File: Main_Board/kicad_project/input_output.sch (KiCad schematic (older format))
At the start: 70 parts

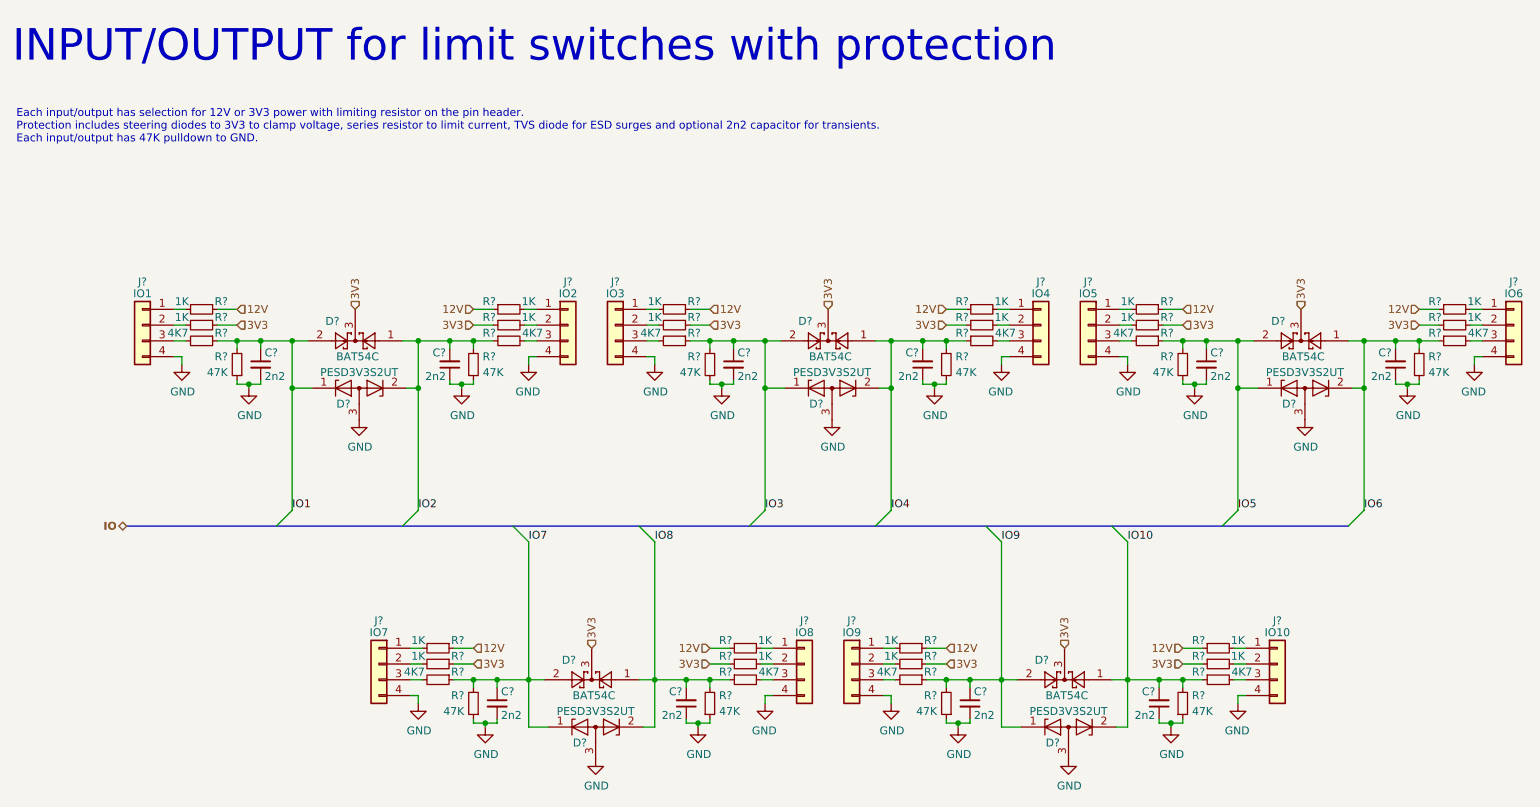
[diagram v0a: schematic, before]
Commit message: Fix I/O protection
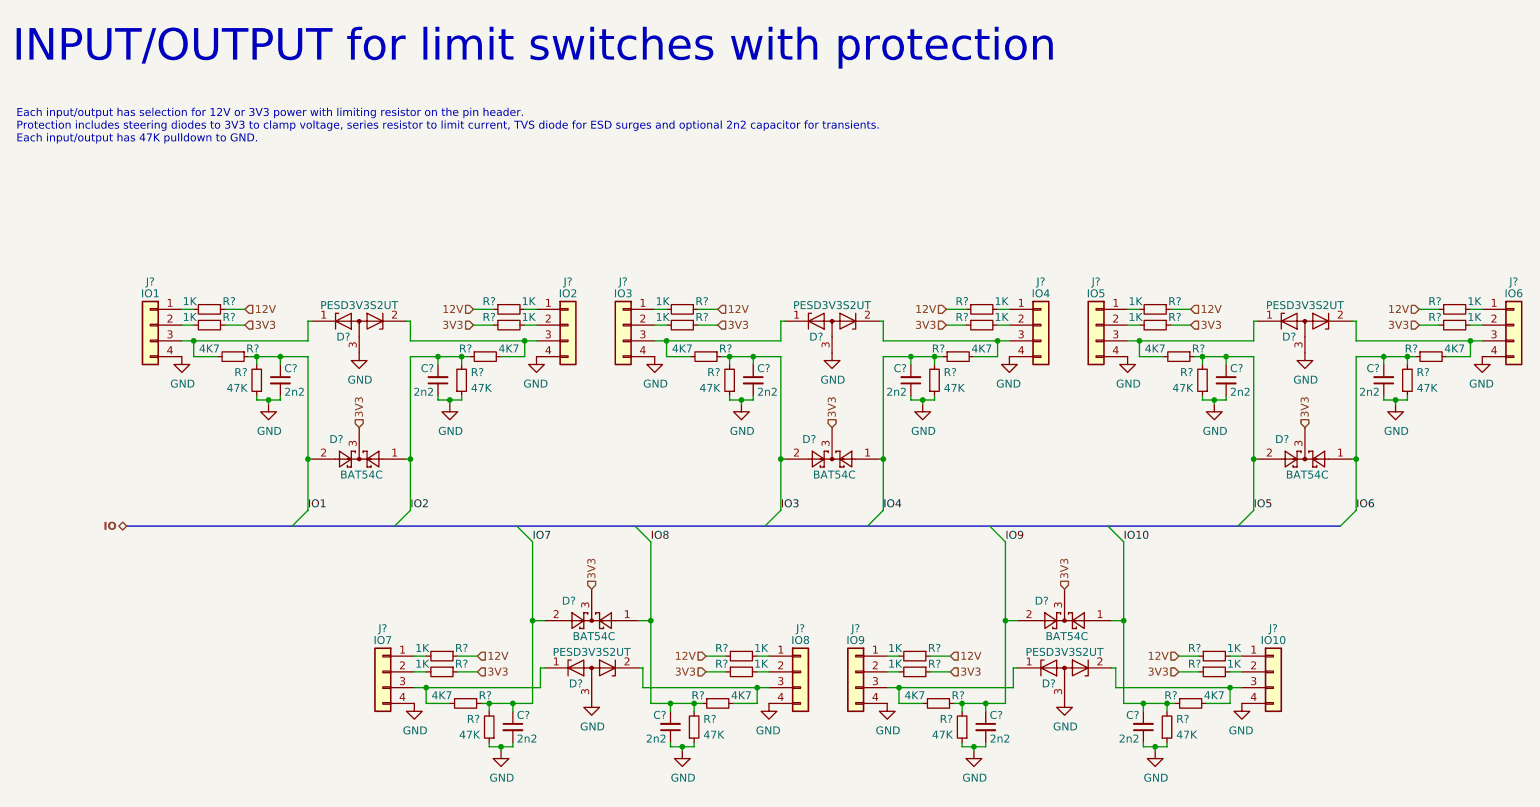
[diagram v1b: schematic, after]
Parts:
- removed C? (x8): 2n2, Capacitor_SMD:C_0603_1608Metric, symbol Device:C_Small
- removed D? (x4): BAT54C, Package_TO_SOT_SMD:SOT-23, symbol Diode:BAT54C
- removed D? (x4): PESD3V3S2UT, Package_TO_SOT_SMD:SOT-23, symbol Device:D_Zener_x2_ACom_KKA
- removed J?: IO3, Connector_PinHeader_2.54mm:PinHeader_1x04_P2.54mm_Vertical, symbol Connector_Generic:Conn_01x04
- removed J?: IO4, Connector_PinHeader_2.54mm:PinHeader_1x04_P2.54mm_Vertical, symbol Connector_Generic:Conn_01x04
- removed J?: IO5, Connector_PinHeader_2.54mm:PinHeader_1x04_P2.54mm_Vertical, symbol Connector_Generic:Conn_01x04
- removed J?: IO6, Connector_PinHeader_2.54mm:PinHeader_1x04_P2.54mm_Vertical, symbol Connector_Generic:Conn_01x04
- removed J?: IO7, Connector_PinHeader_2.54mm:PinHeader_1x04_P2.54mm_Vertical, symbol Connector_Generic:Conn_01x04
- removed J?: IO8, Connector_PinHeader_2.54mm:PinHeader_1x04_P2.54mm_Vertical, symbol Connector_Generic:Conn_01x04
- removed J?: IO9, Connector_PinHeader_2.54mm:PinHeader_1x04_P2.54mm_Vertical, symbol Connector_Generic:Conn_01x04
- removed J?: IO10, Connector_PinHeader_2.54mm:PinHeader_1x04_P2.54mm_Vertical, symbol Connector_Generic:Conn_01x04
- removed R? (x16): 1K, Resistor_SMD:R_0603_1608Metric, symbol Device:R_Small
- removed R? (x8): 4K7, Resistor_SMD:R_0603_1608Metric, symbol Device:R_Small
- removed R? (x8): 47K, Resistor_SMD:R_0603_1608Metric, symbol Device:R_Small
- added C? (x8): 2n2, Capacitor_SMD:C_0603_1608Metric, symbol Device:C_Small
- added D? (x4): BAT54C, Package_TO_SOT_SMD:SOT-23, symbol Diode:BAT54C
- added D? (x4): PESD3V3S2UT, Package_TO_SOT_SMD:SOT-23, symbol Device:D_Zener_x2_ACom_KKA
- added J?: IO3, Connector_PinHeader_2.54mm:PinHeader_1x04_P2.54mm_Vertical, symbol Connector_Generic:Conn_01x04
- added J?: IO4, Connector_PinHeader_2.54mm:PinHeader_1x04_P2.54mm_Vertical, symbol Connector_Generic:Conn_01x04
- added J?: IO6, Connector_PinHeader_2.54mm:PinHeader_1x04_P2.54mm_Vertical, symbol Connector_Generic:Conn_01x04
- added J?: IO5, Connector_PinHeader_2.54mm:PinHeader_1x04_P2.54mm_Vertical, symbol Connector_Generic:Conn_01x04
- added J?: IO7, Connector_PinHeader_2.54mm:PinHeader_1x04_P2.54mm_Vertical, symbol Connector_Generic:Conn_01x04
- added J?: IO8, Connector_PinHeader_2.54mm:PinHeader_1x04_P2.54mm_Vertical, symbol Connector_Generic:Conn_01x04
- added J?: IO9, Connector_PinHeader_2.54mm:PinHeader_1x04_P2.54mm_Vertical, symbol Connector_Generic:Conn_01x04
- added J?: IO10, Connector_PinHeader_2.54mm:PinHeader_1x04_P2.54mm_Vertical, symbol Connector_Generic:Conn_01x04
- added R? (x16): 1K, Resistor_SMD:R_0603_1608Metric, symbol Device:R_Small
- added R? (x8): 4K7, Resistor_SMD:R_0603_1608Metric, symbol Device:R_Small
- added R? (x8): 47K, Resistor_SMD:R_0603_1608Metric, symbol Device:R_Small
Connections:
- net 12V: now also R?.1, R?.1, R?.1, R?.1, R?.1, R?.1, R?.1, R?.1
- net 3V3: now also D?.3, D?.3, D?.3, D?.3, R?.1, R?.1, R?.1, R?.1, R?.1, R?.1, R?.1, R?.1
- net GND: now also C?.1, C?.1, C?.1, C?.1, C?.2, C?.2, C?.2, C?.2, D?.3 (A), D?.3 (A), D?.3 (A), D?.3 (A), J?.4 (Pin_4), J?.4 (Pin_4), J?.4 (Pin_4), J?.4 (Pin_4), J?.4 (Pin_4), J?.4 (Pin_4), J?.4 (Pin_4), J?.4 (Pin_4), R?.1, R?.1, R?.1, R?.1, R?.1, R?.1, R?.1, R?.1
- net IO1: no longer D?.1 (K)
- net IO10: now also C?.2, D?.1, R?.1, R?.2
- net IO2: no longer D?.2 (K)
- net IO3: now also C?.1, D?.2, R?.1, R?.2
- net IO4: now also C?.2, D?.1, R?.1, R?.2
- net IO5: now also C?.1, D?.2, R?.1, R?.2
- net IO6: now also C?.2, D?.1, R?.1, R?.2
- net IO7: now also C?.1, D?.2, R?.1, R?.2
- net IO8: now also C?.2, D?.1, R?.1, R?.2
- net IO9: now also C?.1, D?.2, R?.1, R?.2
- net at J?.3 (Pin_3), R?.2: now also D?.1 (K)
- net at J?.3 (Pin_3), R?.2: now also D?.2 (K)
- new net: J?.1 (Pin_1), R?.2 (x8)
- new net: J?.2 (Pin_2), R?.2 (x8)
- new net: D?.1 (K), J?.3 (Pin_3), R?.2 (x4)
- new net: D?.2 (K), J?.3 (Pin_3), R?.2 (x4)
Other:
- moved on the sheet: C?, D?, J?, R?
